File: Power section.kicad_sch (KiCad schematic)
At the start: 17 parts, among them J2 USB3_A, U4 TLV76733, U5 USBLC6-2P6, U6 TPS7A0212

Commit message: 1. net class assigned to all the nets 2.Slight placement changes
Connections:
- net _P: now reaches R4.1, U5.6 (I/O1)
- net _N: now reaches R5.1, U5.4 (I/O2)
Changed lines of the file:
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@@
+		)
+	)
+	(label "_N"
+		(at 81.28 45.72 0)
+		(effects
+			(font
+				(size 1.27 1.27)
+			)
+			(justify left bottom)
 		)
 	)
@@
 		)
 	)
+	(label "_P"
+		(at 81.28 43.18 0)
+		(effects
+			(font
+				(size 1.27 1.27)
+			)
+			(justify left bottom)
+		)
+	)

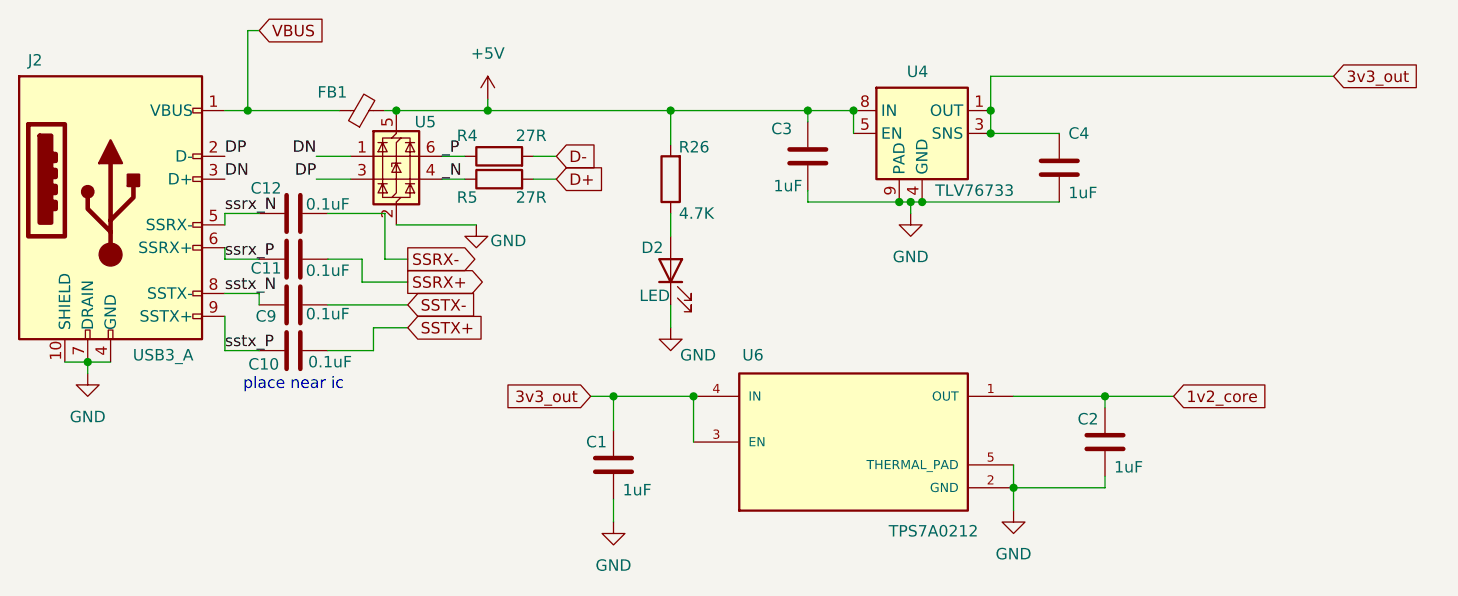
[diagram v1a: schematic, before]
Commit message: 1. Major routing done- usb3.1,usb2, >> 2. buck converter and voltage regulators placement and routing done >> 3. Decoupling caps added
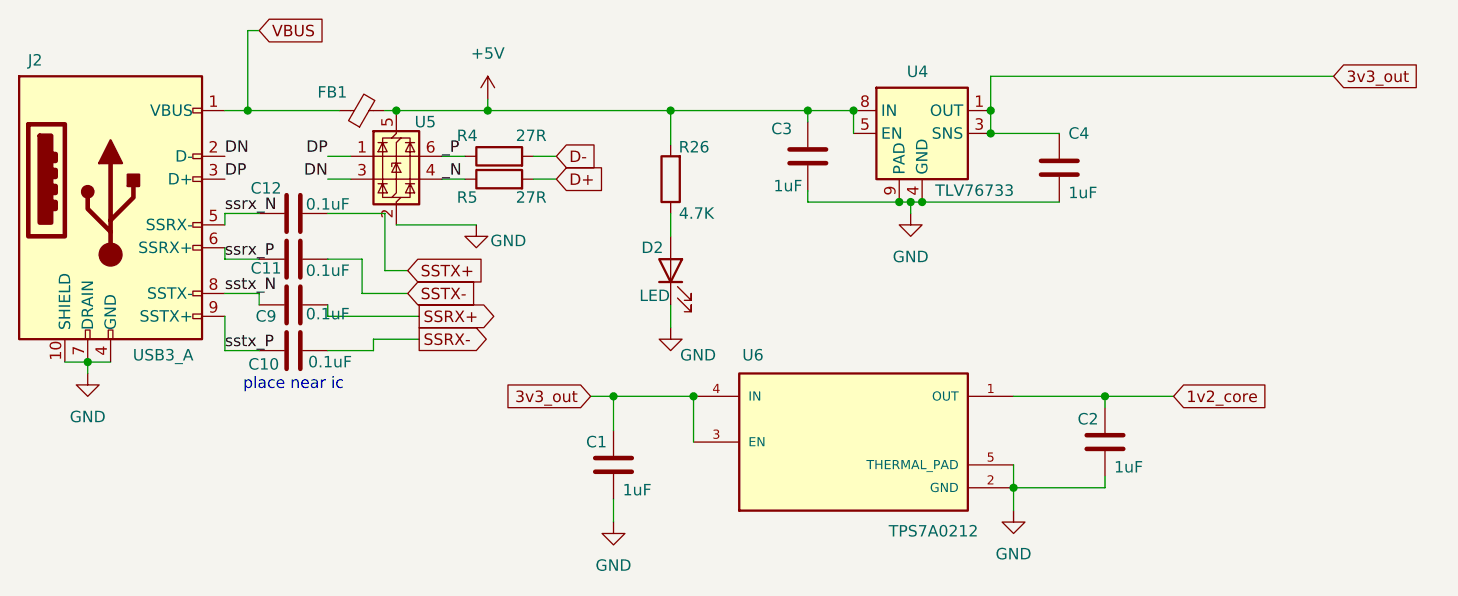
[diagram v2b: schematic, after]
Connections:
- net DN: now also J2.2 (D-), U5.3 (I/O2); no longer J2.3 (D+), U5.1 (I/O1)
- net DP: now also J2.3 (D+), U5.1 (I/O1); no longer J2.2 (D-), U5.3 (I/O2)
- net SSRX+: now also C9.2; no longer C11.2
- net SSRX-: now also C10.2; no longer C12.2
- net SSTX+: now also C12.2; no longer C10.2
- net SSTX-: now also C11.2; no longer C9.2
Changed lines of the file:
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@@
 	(wire
 		(pts
-			(xy 77.47 54.61) (xy 74.93 54.61)
+			(xy 73.66 63.5) (xy 73.66 64.77)
+		)
+		(stroke
+			(width 0)
+			(type default)
+		)
+	)
+	(wire
+		(pts
+			(xy 68.58 60.96) (xy 78.74 60.96)
+		)
+		(stroke
+			(width 0)
+			(type default)
+		)
+	)
+	(wire
+		(pts
+			(xy 68.58 45.72) (xy 71.12 45.72)
 		)
 		(stroke
@@
 	(wire
 		(pts
-			(xy 67.31 45.72) (xy 71.12 45.72)
-		)
-		(stroke
-			(width 0)
-			(type default)
-		)
-	)
-	(wire
-		(pts
 			(xy 121.92 48.26) (xy 132.08 48.26)
 		)
@@
 	(wire
 		(pts
-			(xy 72.39 57.15) (xy 77.47 57.15)
-		)
-		(stroke
-			(width 0)
-			(type default)
-		)
-	)
-	(wire
-		(pts
 			(xy 41.91 67.31) (xy 41.91 66.04)
 		)
@@
 	(wire
 		(pts
+			(xy 72.39 54.61) (xy 72.39 58.42)
+		)
+		(stroke
+			(width 0)
+			(type default)
+		)
+	)
+	(wire
+		(pts
 			(xy 100.33 81.28) (xy 100.33 83.82)
 		)
@@
 	(wire
 		(pts
+			(xy 77.47 55.88) (xy 74.93 55.88)
+		)
+		(stroke
+			(width 0)
+			(type default)
+		)
+	)
+	(wire
+		(pts
 			(xy 121.92 46.99) (xy 121.92 48.26)
 		)
@@
 	(wire
 		(pts
-			(xy 73.66 62.23) (xy 77.47 62.23)
-		)
-		(stroke
-			(width 0)
-			(type default)
-		)
-	)
-	(wire
-		(pts
-			(xy 74.93 54.61) (xy 74.93 49.53)
+			(xy 68.58 43.18) (xy 71.12 43.18)
+		)
+		(stroke
+			(width 0)
+			(type default)
+		)
+	)
+	(wire
+		(pts
+			(xy 74.93 49.53) (xy 74.93 55.88)
 		)
 		(stroke
@@
 	(wire
 		(pts
+			(xy 72.39 58.42) (xy 77.47 58.42)
+		)
+		(stroke
+			(width 0)
+			(type default)
+		)
+	)
+	(wire
+		(pts
 			(xy 121.92 38.1) (xy 127 38.1)
 		)
@@
 	(wire
 		(pts
-			(xy 72.39 54.61) (xy 72.39 57.15)
-		)
-		(stroke
-			(width 0)
-			(type default)
-		)
-	)
-	(wire
-		(pts
 			(xy 57.15 64.77) (xy 60.96 64.77)
 		)
@@
 	(wire
 		(pts
-			(xy 68.58 59.69) (xy 77.47 59.69)
-		)
-		(stroke
-			(width 0)
-			(type default)
-		)
-	)
-	(wire
-		(pts
 			(xy 109.22 69.85) (xy 109.22 74.93)
 		)
@@
 	(wire
 		(pts
+			(xy 68.58 59.69) (xy 68.58 60.96)
+		)
+		(stroke
+			(width 0)
+			(type default)
+		)
+	)
+	(wire
+		(pts
 			(xy 180.34 34.29) (xy 142.24 34.29)
 		)
@@
 	(wire
 		(pts
-			(xy 73.66 64.77) (xy 73.66 62.23)
-		)
-		(stroke
-			(width 0)
-			(type default)
-		)
-	)
-	(wire
-		(pts
 			(xy 144.78 77.47) (xy 144.78 80.01)
 		)
@@
 	(wire
 		(pts
-			(xy 67.31 43.18) (xy 71.12 43.18)
-		)
-		(stroke
-			(width 0)
-			(type default)
-		)
-	)
-	(wire
-		(pts
 			(xy 121.92 38.1) (xy 121.92 39.37)
+		)
+		(stroke
+			(width 0)
+			(type default)
+		)
+	)
+	(wire
+		(pts
+			(xy 73.66 63.5) (xy 78.74 63.5)
 		)
 		(stroke
@@
 	)
 	(label "DN"
+		(at 57.15 43.18 0)
+		(effects
+			(font
+				(size 1.27 1.27)
+			)
+			(justify left bottom)
+		)
+	)
+	(label "DP"
 		(at 57.15 45.72 0)
-		(effects
-			(font
-				(size 1.27 1.27)
-			)
-			(justify left bottom)
-		)
-	)
-	(label "DP"
-		(at 57.15 43.18 0)
 		(effects
 			(font
@@
 	)
 	(label "DP"
-		(at 67.31 45.72 180)
+		(at 68.58 43.18 180)
 		(effects
 			(font
@@
 	)
 	(label "DN"
-		(at 67.31 43.18 180)
+		(at 68.58 45.72 180)
 		(effects
 			(font
@@
 	(global_label "SSRX+"
 		(shape output)
-		(at 77.47 57.15 0)
+		(at 78.74 60.96 0)
 		(fields_autoplaced yes)
 		(effects
@@
 		)
 		(property "Intersheetrefs" "${INTERSHEET_REFS}"
-			(at 86.9261 57.15 0)
+			(at 88.1961 60.96 0)
 			(show_name no)
 			(do_not_autoplace no)
@@
 	(global_label "SSRX-"
 		(shape output)
-		(at 77.47 54.61 0)
+		(at 78.74 63.5 0)
 		(fields_autoplaced yes)
 		(effects
@@
 		)
 		(property "Intersheetrefs" "${INTERSHEET_REFS}"
-			(at 86.9261 54.61 0)
+			(at 88.1961 63.5 0)
 			(show_name no)
 			(do_not_autoplace no)
@@
 		)
 	)
-	(global_label "SSTX+"
+	(global_label "SSTX-"
 		(shape input)
-		(at 77.47 62.23 0)
+		(at 77.47 58.42 0)
 		(fields_autoplaced yes)
 		(effects
@@
 		)
 		(property "Intersheetrefs" "${INTERSHEET_REFS}"
-			(at 86.6237 62.23 0)
+			(at 86.6237 58.42 0)
 			(show_name no)
 			(do_not_autoplace no)
@@
 		)
 	)
-	(global_label "SSTX-"
+	(global_label "SSTX+"
 		(shape input)
-		(at 77.47 59.69 0)
+		(at 77.47 55.88 0)
 		(fields_autoplaced yes)
 		(effects
@@
 		)
 		(property "Intersheetrefs" "${INTERSHEET_REFS}"
-			(at 86.6237 59.69 0)
+			(at 86.6237 55.88 0)
 			(show_name no)
 			(do_not_autoplace no)

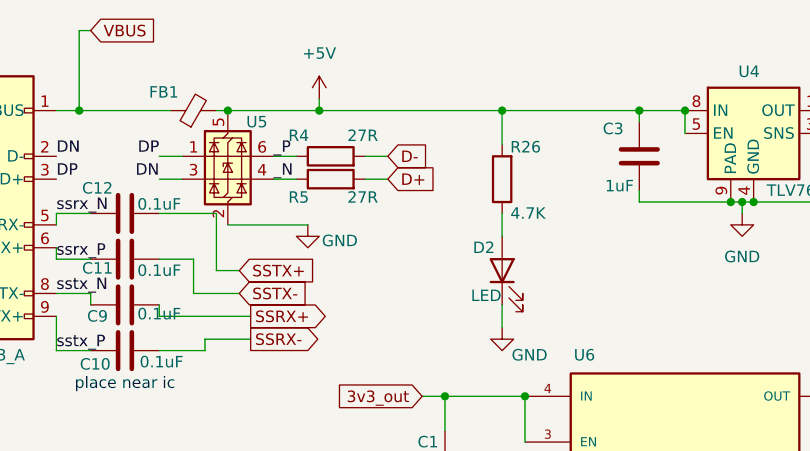
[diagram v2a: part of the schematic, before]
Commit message: 1. usb routing done 2.clock routing done 3. decoupling capacitors(3.3v) routing for lan7801 ic done
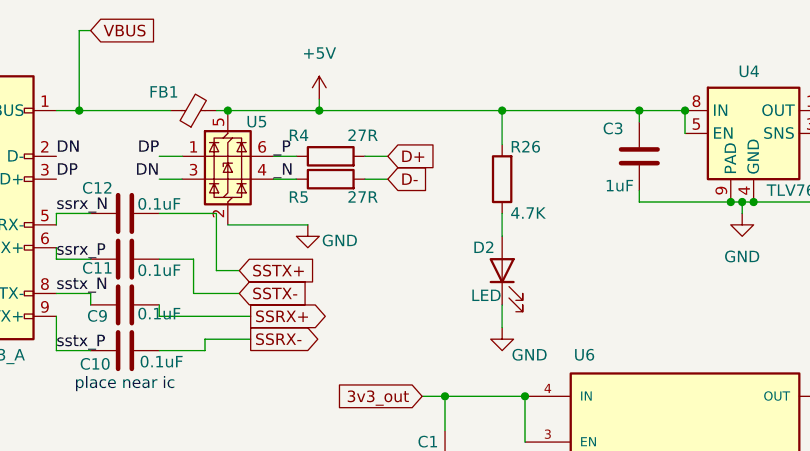
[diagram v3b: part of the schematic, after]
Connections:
- net D+: now also R4.2; no longer R5.2
- net D-: now also R5.2; no longer R4.2
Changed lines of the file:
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@@
+	(wire
+		(pts
+			(xy 93.98 45.72) (xy 91.44 45.72)
+		)
+		(stroke
+			(width 0)
+			(type default)
+		)
+	)
 	(wire
 		(pts
@@
 	(wire
 		(pts
-			(xy 91.44 45.72) (xy 93.98 45.72)
-		)
-		(stroke
-			(width 0)
-			(type default)
-		)
-	)
-	(wire
-		(pts
 			(xy 68.58 59.69) (xy 68.58 60.96)
 		)
@@
 	(wire
 		(pts
-			(xy 91.44 43.18) (xy 93.98 43.18)
-		)
-		(stroke
-			(width 0)
-			(type default)
-		)
-	)
-	(wire
-		(pts
 			(xy 144.78 77.47) (xy 144.78 80.01)
 		)
@@
 		(pts
 			(xy 39.37 66.04) (xy 41.91 66.04)
+		)
+		(stroke
+			(width 0)
+			(type default)
+		)
+	)
+	(wire
+		(pts
+			(xy 93.98 43.18) (xy 91.44 43.18)
 		)
 		(stroke
@@
 	(global_label "D-"
 		(shape input)
-		(at 93.98 43.18 0)
+		(at 93.98 45.72 0)
 		(fields_autoplaced yes)
 		(effects
@@
 		)
 		(property "Intersheetrefs" "${INTERSHEET_REFS}"
-			(at 99.8076 43.18 0)
+			(at 99.8076 45.72 0)
 			(show_name no)
 			(do_not_autoplace no)
@@
 	(global_label "D+"
 		(shape input)
-		(at 93.98 45.72 0)
+		(at 93.98 43.18 0)
 		(fields_autoplaced yes)
 		(effects
@@
 		)
 		(property "Intersheetrefs" "${INTERSHEET_REFS}"
-			(at 99.8076 45.72 0)
+			(at 99.8076 43.18 0)
 			(show_name no)
 			(do_not_autoplace no)
